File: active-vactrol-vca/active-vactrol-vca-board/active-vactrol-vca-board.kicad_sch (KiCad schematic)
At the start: 14 parts, among them U1 TL072, U2 TL072, U3 TL072, U4 TL072, U7 AMS1117-5.0

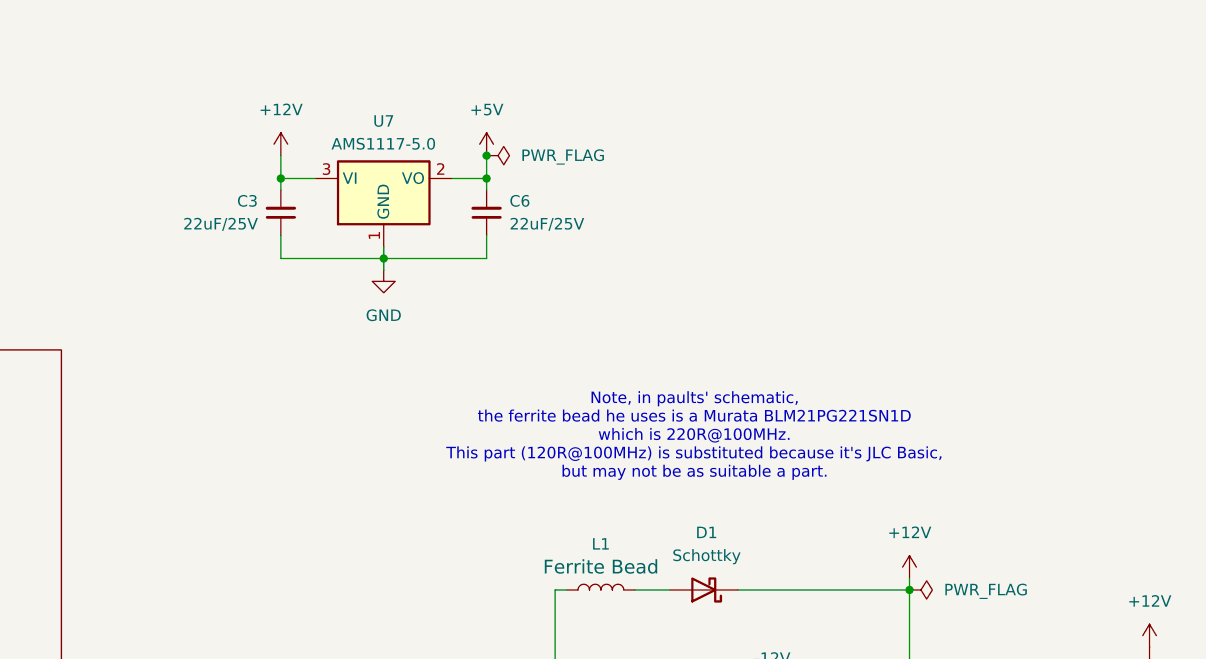
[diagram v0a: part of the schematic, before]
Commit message: Adds v1.0 of Crustose and updates Vactrol VCA for production. Updates Lichen symbol and footprint library..
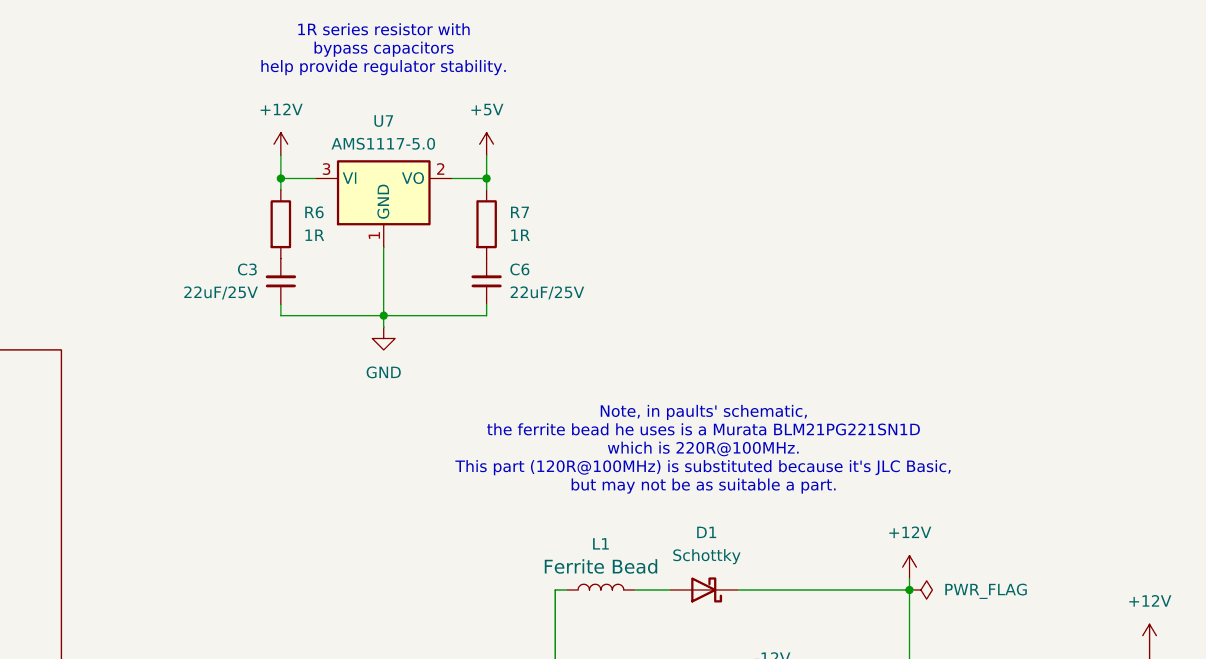
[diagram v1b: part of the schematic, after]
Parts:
- added R6, R7: 1R, Lichen:R_0603, symbol Lichen:1R_0603
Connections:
- net +12V: now also R6.1; no longer C3.2
- net +5V: now also R7.1; no longer C6.2
- new net: C6.2, R7.2
- new net: C3.2, R6.2
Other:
- note added: "1R series resistor with bypass capacitors help provide regulator stability."
- moved on the sheet: C3, C6

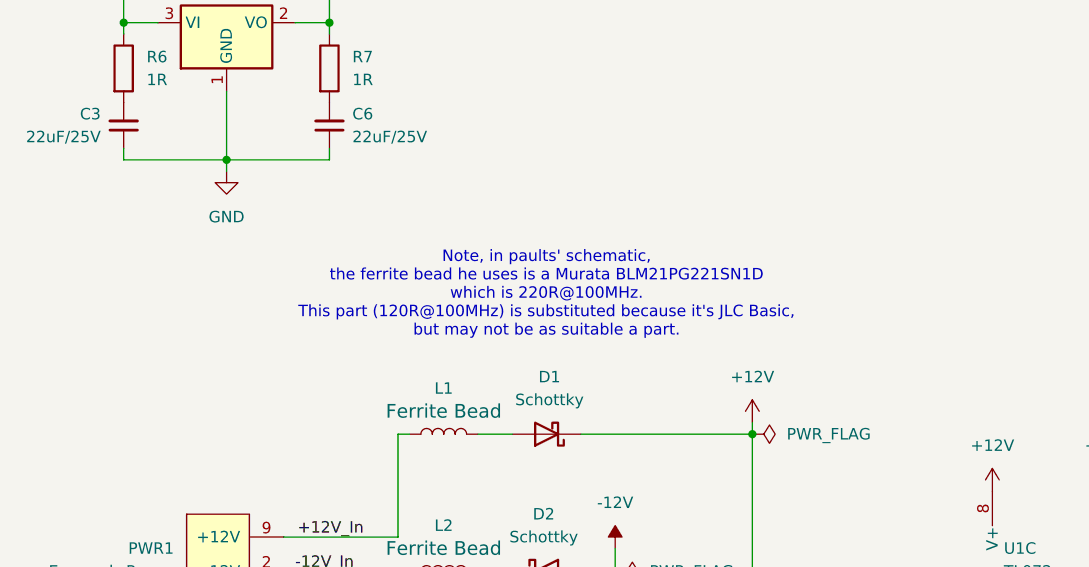
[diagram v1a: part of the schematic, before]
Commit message: Updates Lichen symbols and footprints. Fixes to Crustose and Vactrol VCA. Adds 3D model of the RP2350 dual USB board.
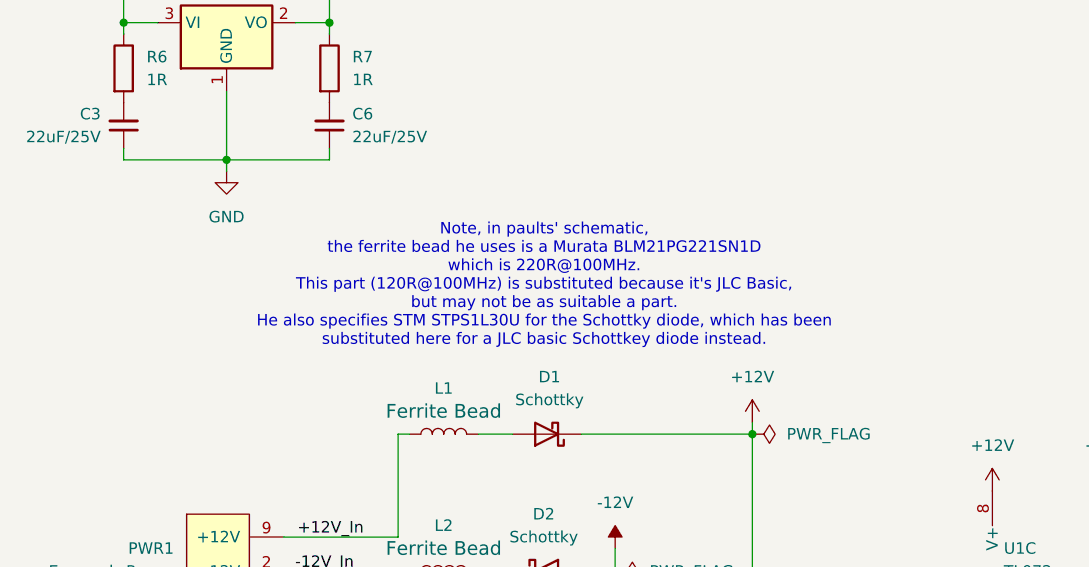
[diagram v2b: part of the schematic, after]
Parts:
- D1: footprint Diode_SMD:D_SMB_Handsoldering -> Diode_SMD:D_SMA_Handsoldering; symbol Lichen:Schottky_Diode -> Lichen:Schottky_Diode_JLC_Basic; JLCPCB ID C222239 -> (none); LCSC (none) -> C8678; Manufacturer STMicroelectronics -> MDD(Microdiode Semiconductor); Part Number STPS1L30U -> SS34
- D2: footprint Diode_SMD:D_SMB_Handsoldering -> Diode_SMD:D_SMA_Handsoldering; symbol Lichen:Schottky_Diode -> Lichen:Schottky_Diode_JLC_Basic; JLCPCB ID C222239 -> (none); LCSC C222239 -> C8678; Manufacturer STMicroelectronics -> MDD(Microdiode Semiconductor); Part Number STPS1L30U -> SS34
- PWR1: now left out of the parts list
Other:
- note added: "Note, in paults' schematic, the ferrite bead he uses is a Murata BLM21PG221SN1D which is 220R@100MHz. This part (120R@100MHz) is substituted because it's JLC Basic, but may not be as suitable a part. He also specifies STM STPS1L30U for the Schottky diode, which has been substituted here for a JLC basic Schottkey diode instead."
- note removed: "Note, in paults' schematic, the ferrite bead he uses is a Murata BLM21PG221SN1D which is 220R@100MHz. This part (120R@100MHz) is substituted because it's JLC Basic, but may not be as suitable a part."
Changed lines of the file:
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@@
 		)
 	)
-	(text "Note, in paults' schematic,\nthe ferrite bead he uses is a Murata BLM21PG221SN1D\nwhich is 220R@100MHz.\nThis part (120R@100MHz) is substituted because it's JLC Basic,\nbut may not be as suitable a part."
+	(text "Note, in paults' schematic,\nthe ferrite bead he uses is a Murata BLM21PG221SN1D\nwhich is 220R@100MHz.\nThis part (120R@100MHz) is substituted because it's JLC Basic,\nbut may not be as suitable a part.\nHe also specifies STM STPS1L30U for the Schottky diode, which has been\nsubstituted here for a JLC basic Schottkey diode instead."
 		(exclude_from_sim no)
-		(at 165.1 72.136 0)
+		(at 164.846 71.12 0)
 		(effects
 			(font
@@
 		(unit 1)
 		(exclude_from_sim no)
-		(in_bom yes)
+		(in_bom no)
 		(on_board yes)
 		(dnp no)
@@
 	)
 	(symbol
-		(lib_id "Lichen:Schottky_Diode")
+		(lib_id "Lichen:Schottky_Diode_JLC_Basic")
 		(at 165.1 87.63 180)
 		(unit 1)
@@
 			)
 		)
-		(property "Footprint" "Diode_SMD:D_SMB_Handsoldering"
+		(property "Footprint" "Diode_SMD:D_SMA_Handsoldering"
 			(at 165.1 87.63 0)
 			(effects
@@
 			)
 		)
-		(property "Datasheet" "https://www.lcsc.com/datasheet/lcsc_datasheet_2409301604_STMicroelectronics-STPS1L30U_C222239.pdf"
+		(property "Datasheet" "https://jlcpcb.com/api/file/downloadByFileSystemAccessId/8586172667489079296"
 			(at 165.1 87.63 0)
 			(effects
@@
 			)
 		)
-		(property "Manufacturer" "STMicroelectronics"
+		(property "Manufacturer" "MDD(Microdiode Semiconductor)"
 			(at 165.1 87.63 0)
 			(effects
@@
 			)
 		)
-		(property "Part Number" "STPS1L30U"
+		(property "Part Number" "SS34"
 			(at 165.1 87.63 0)
 			(effects
@@
 			)
 		)
-		(property "JLCPCB ID" "C222239"
+		(property "LCSC" "C8678"
 			(at 165.1 87.63 0)
 			(effects
@@
 	)
 	(symbol
-		(lib_id "Lichen:Schottky_Diode")
+		(lib_id "Lichen:Schottky_Diode_JLC_Basic")
 		(at 165.1 102.87 0)
 		(unit 1)
@@
 			)
 		)
-		(property "Footprint" "Diode_SMD:D_SMB_Handsoldering"
+		(property "Footprint" "Diode_SMD:D_SMA_Handsoldering"
 			(at 165.1 102.87 0)
 			(effects
@@
 			)
 		)
-		(property "Datasheet" "https://www.lcsc.com/datasheet/lcsc_datasheet_2409301604_STMicroelectronics-STPS1L30U_C222239.pdf"
+		(property "Datasheet" "https://jlcpcb.com/api/file/downloadByFileSystemAccessId/8586172667489079296"
 			(at 165.1 102.87 0)
 			(effects
@@
 			)
 		)
-		(property "Manufacturer" "STMicroelectronics"
+		(property "Manufacturer" "MDD(Microdiode Semiconductor)"
 			(at 165.1 102.87 0)
 			(effects
@@
 			)
 		)
-		(property "Part Number" "STPS1L30U"
+		(property "Part Number" "SS34"
 			(at 165.1 102.87 0)
 			(effects
@@
 			)
 		)
-		(property "LCSC" "C222239"
+		(property "LCSC" "C8678"
 			(at 165.1 102.87 0)
 			(effects
-				(font
-					(size 1.27 1.27)
-				)
-				(hide yes)
-			)
-		)
-		(property "JLCPCB ID" "C222239"
-			(at 165.1 102.87 0)
-			(effects
